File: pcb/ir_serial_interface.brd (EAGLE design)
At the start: 41.6 x 25.4 mm, 27 parts, among them IC1 PIC18F2550_28W, IC2 LP2992, Q2 BC847SMD, T1 SFH303

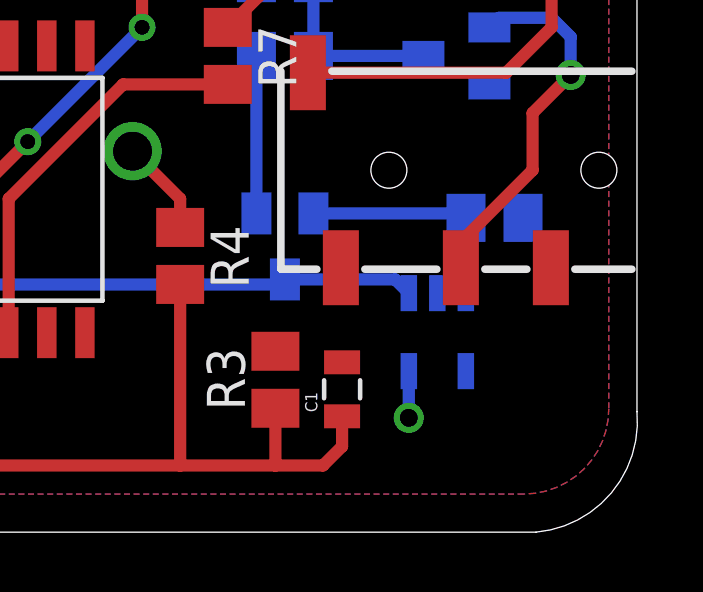
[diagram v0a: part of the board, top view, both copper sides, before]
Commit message: PCB: missing routes
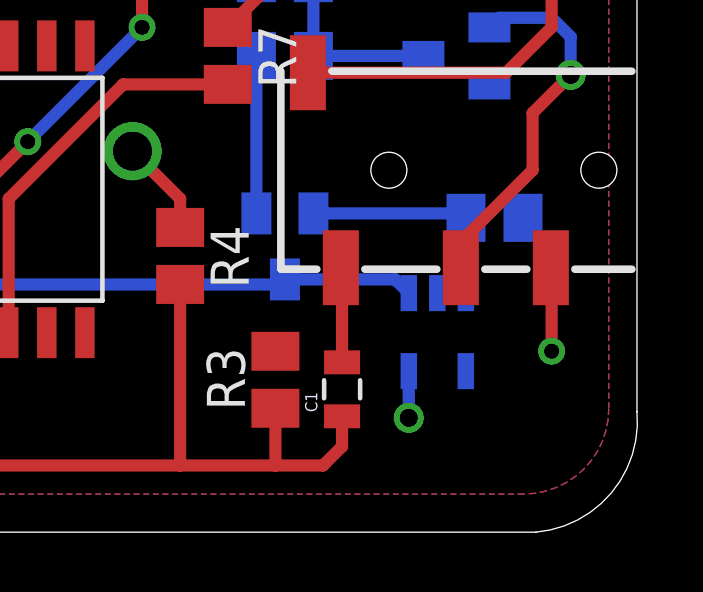
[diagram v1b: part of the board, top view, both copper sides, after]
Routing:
- net N$5: track 0.00 -> 3.19 mm
- net GND: track 23.9 -> 26.7 mm, vias 3 -> 4
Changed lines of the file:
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@@
 <wire x1="46.355" y1="38.1" x2="47.9425" y2="36.5125" width="0.4064" layer="1"/>
 <wire x1="47.9425" y1="36.5125" x2="47.9425" y2="35.5575" width="0.4064" layer="1"/>
-<wire x1="59.37" y1="35.8775" x2="60.3" y2="34.215" width="0" layer="19" extent="1-16"/>
+<wire x1="60.3" y1="34.215" x2="60.325" y2="34.215" width="0.4064" layer="1"/>
+<wire x1="60.325" y1="34.215" x2="60.325" y2="31.4325" width="0.4064" layer="1"/>
+<via x="60.325" y="31.4325" extent="1-16" drill="0.5"/>
 </signal>
 <signal name="N$1">
@@
 <contactref element="U$2" pad="TIP"/>
 <contactref element="C1" pad="2"/>
-<wire x1="53.34" y1="31.0625" x2="53.3" y2="34.215" width="0" layer="19" extent="1-1"/>
+<wire x1="53.3" y1="34.215" x2="53.34" y2="34.215" width="0.4064" layer="1"/>
+<wire x1="53.34" y1="34.215" x2="53.34" y2="31.0625" width="0.4064" layer="1"/>
 </signal>
 <signal name="N$11">

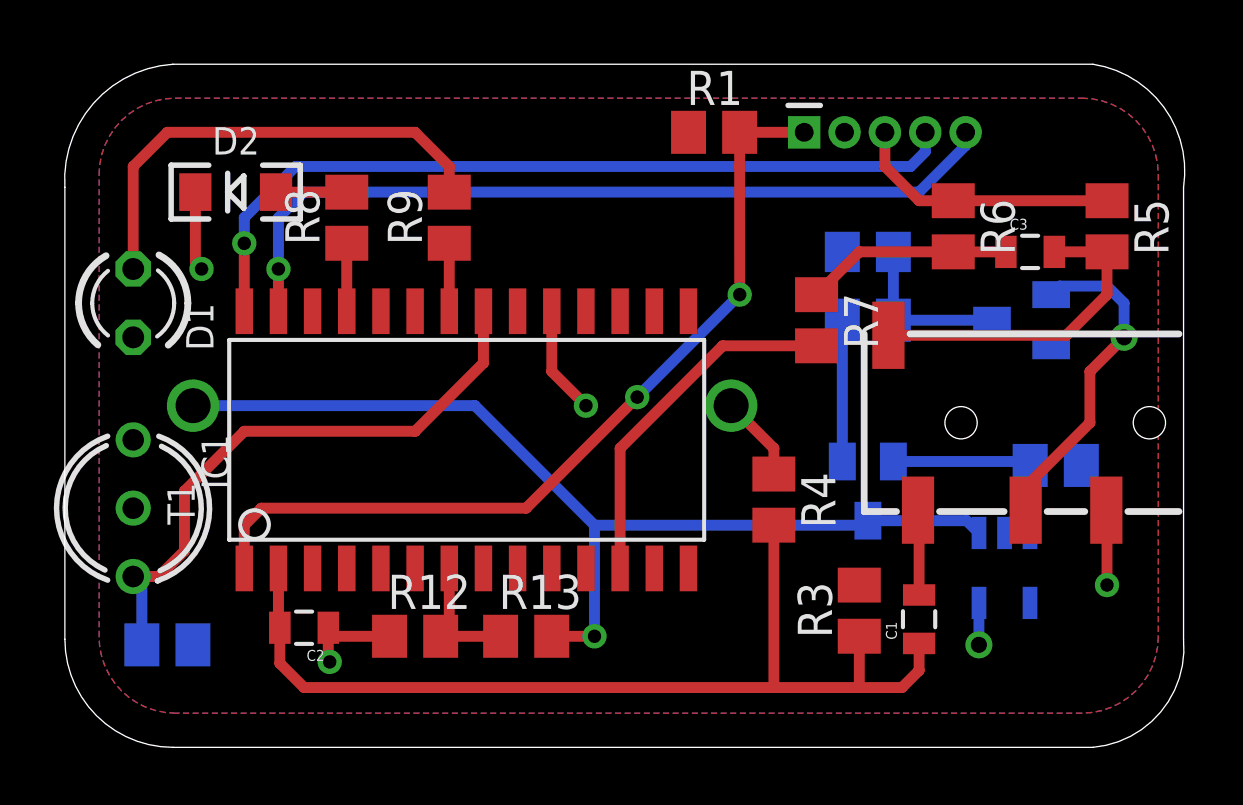
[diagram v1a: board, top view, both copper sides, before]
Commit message: cut round - wider outline path
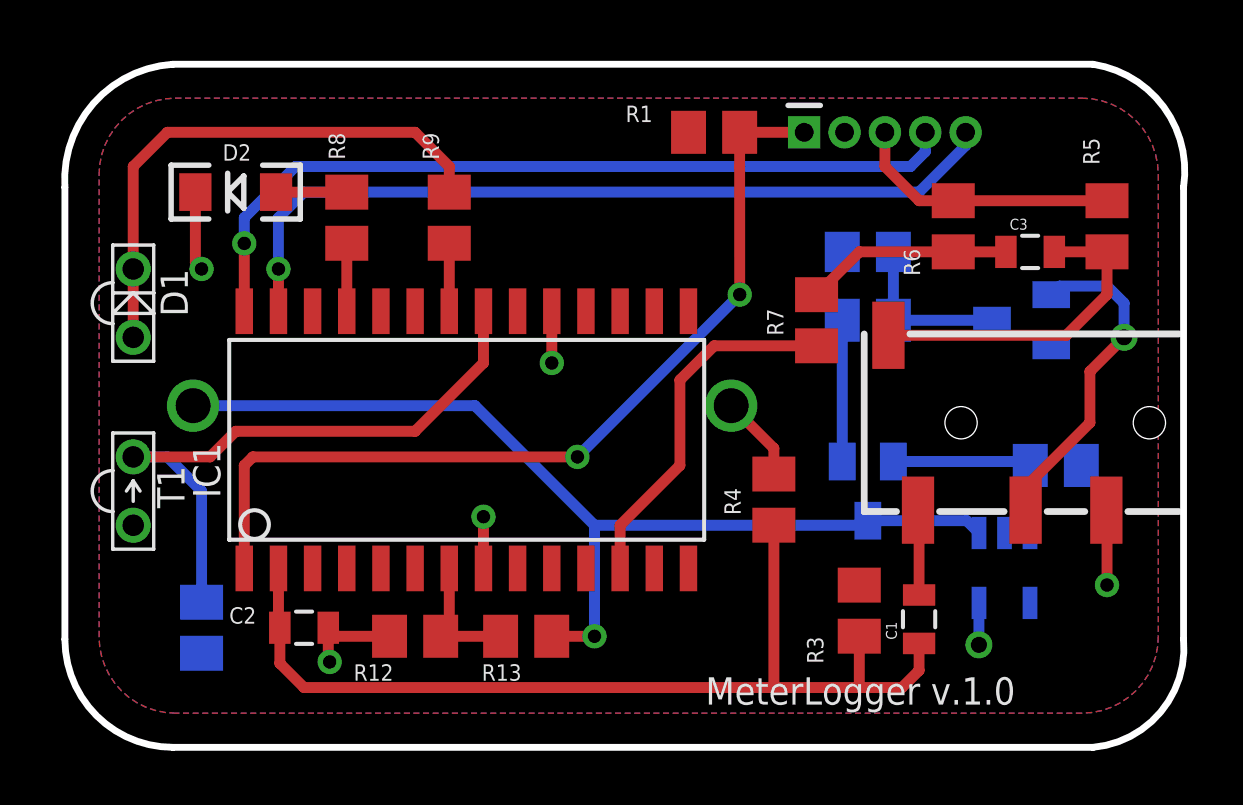
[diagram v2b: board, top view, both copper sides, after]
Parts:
- D1: device led:LED3MM -> SparkFun-LED:LTE-302
- T1: value SFH303 -> PS401; device opto-trans-siemens:SFH303 -> SparkFun-Sensors:LTR-301
- moved R2 1.42 mm to (26.7, 29.8), turned to 90 degrees
- moved T1 0.63 mm to (24.1, 34.9), turned to 270 degrees
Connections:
- removed net VSS: IC1.8
- net +5V: now also T1.C; no longer T1.2
- net GND: now also D1.C, IC1.8; no longer D1.K
- net N$1: now also T1.E; no longer T1.1
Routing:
- net N$14: track 17.6 -> 20.1 mm
- net N$1: track 22.2 -> 23.6 mm
- net N$2: track 32.0 -> 33.3 mm
- net GND: track 26.7 -> 26.6 mm, vias 4 -> 5
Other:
- board text added: "(C) 2014, Kristoffer Ek + Johannes Gaardsted Jørgensen"
- board text added: "2 x CR2032"
- board text added: "MeterLogger v.1.0"

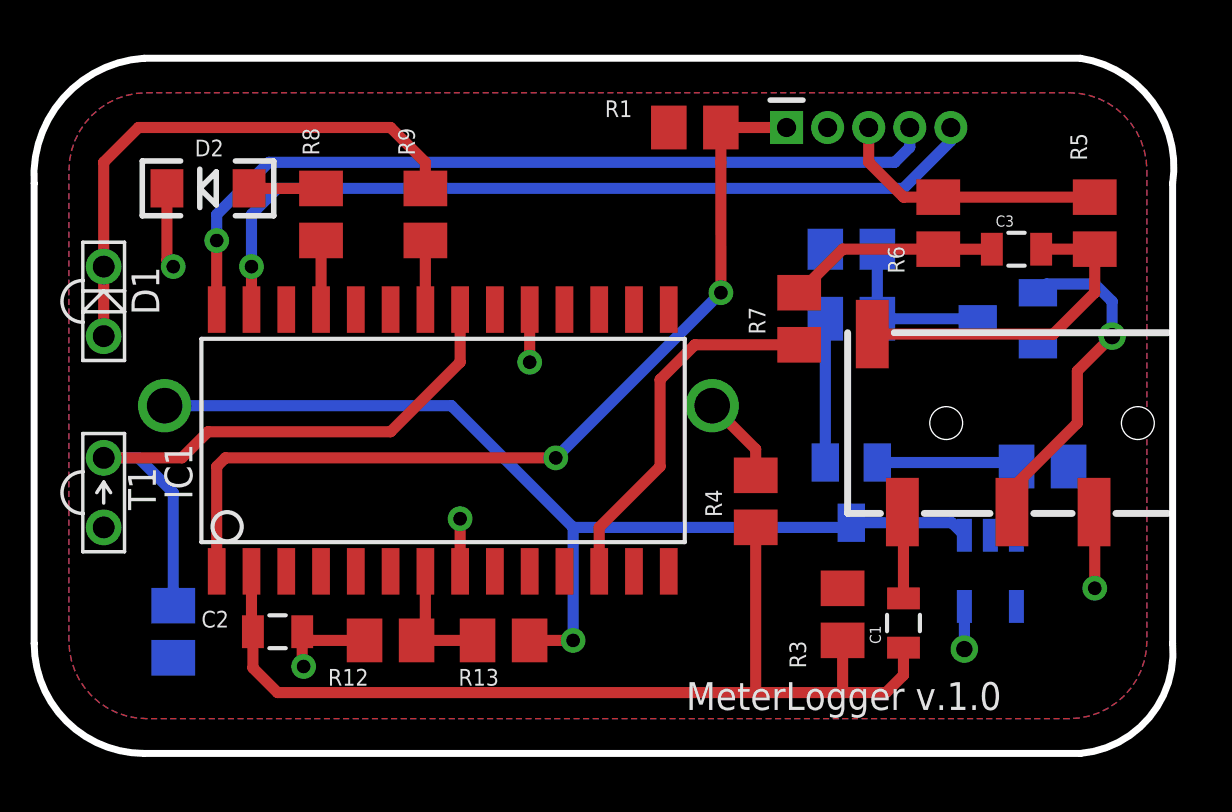
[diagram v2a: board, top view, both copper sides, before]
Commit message: silk screen on name layer not value layer
+ component values
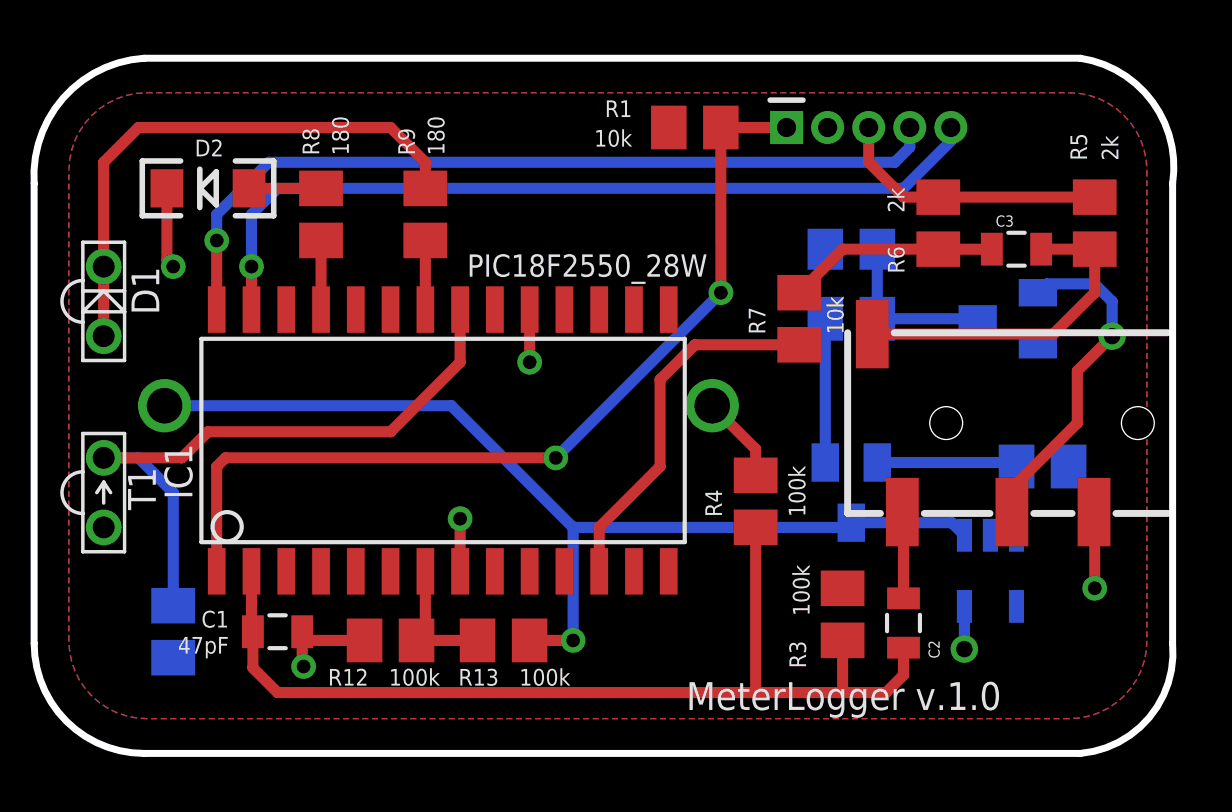
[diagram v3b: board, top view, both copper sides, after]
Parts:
- C1: value 0.2uF -> 47pF
- C2: value 47pF -> 220nF
- C3: value 0.2uF -> 220nF
- C4: value (none) -> 220nF
- D3: value (none) -> BAT65-05; device semicon-smd-ipc:SOT23 -> diode:SOT23
- Q2: value BC847SMD -> MMBT6428LT1G
- R8, R9: value 190 -> 180
- moved C1 22.9 mm to (30.5, 29.8), turned to 180 degrees
- moved C2 22.9 mm to (53.3, 30.2), turned to 90 degrees
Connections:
- net GND: now also C1.1; no longer C2.1
- net N$5: now also C2.2; no longer C1.2
- net N$6: now also C1.2, C2.1; no longer C1.1, C2.2

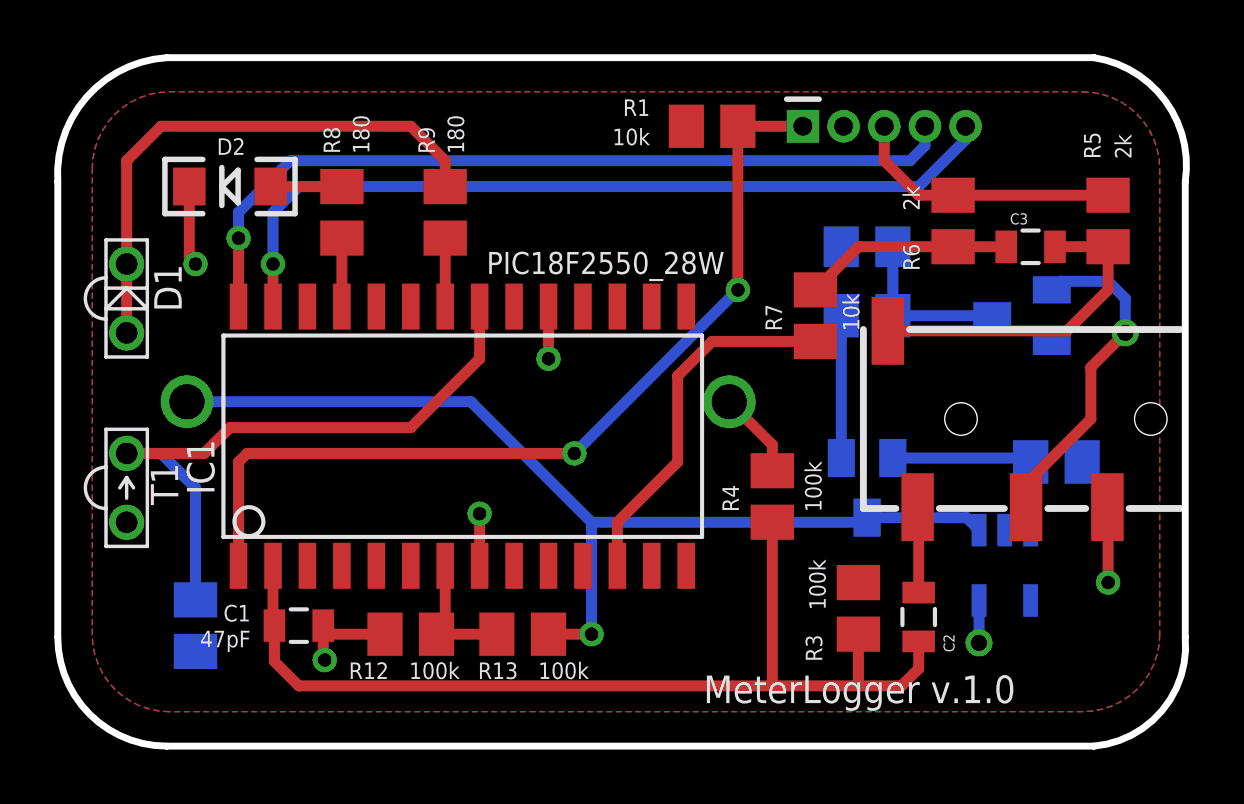
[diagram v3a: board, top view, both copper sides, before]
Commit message: PCB: silk complete
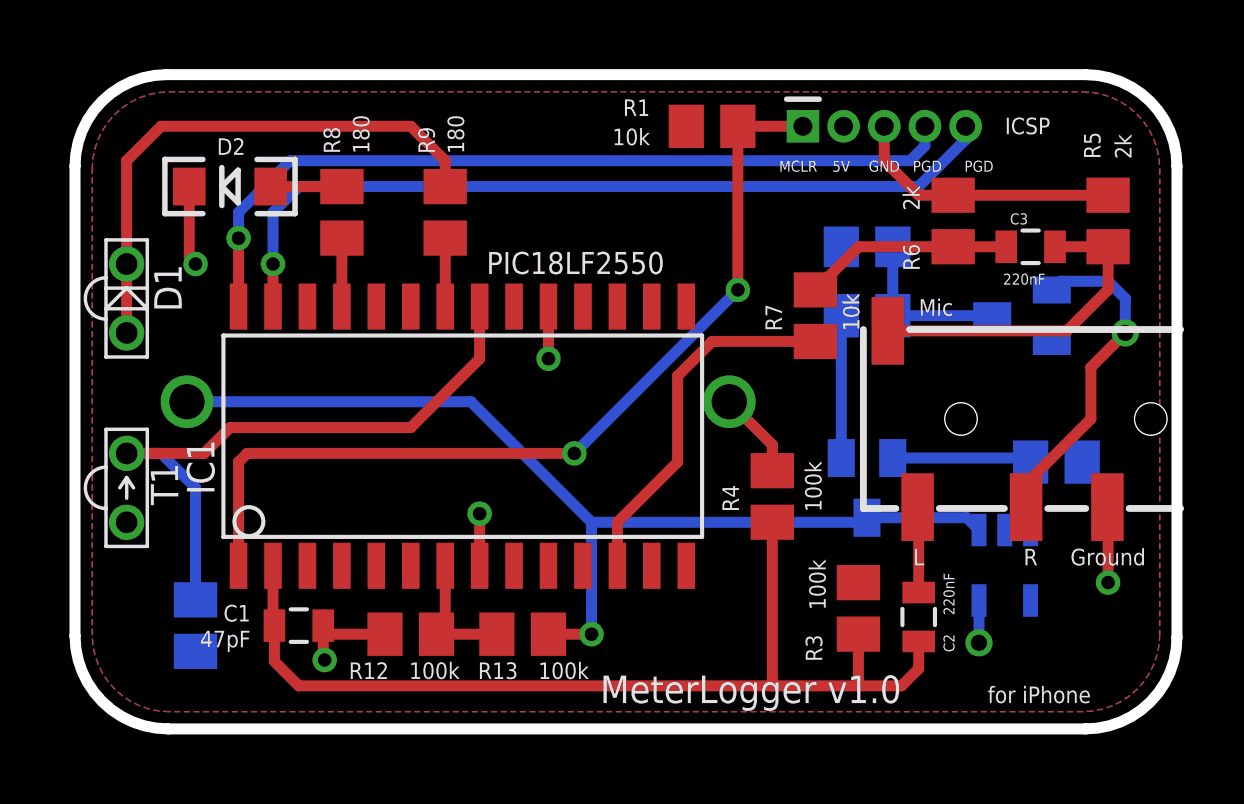
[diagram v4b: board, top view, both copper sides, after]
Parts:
- IC1: value PIC18F2550_28W -> PIC18LF2550
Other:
- board size 41.6 x 25.4 mm -> 40.6 x 24.1 mm
- board text added: "5V"
- board text added: "GND"
- board text added: "Ground"
- board text added: "ICSP"
- board text added: "L"
- board text added: "MCLR"
- board text added: "MeterLogger v1.0"
- board text added: "Mic"
- board text added: "PGD"
- board text added: "R"
- board text added: "for iPhone"
- board text removed: "MeterLogger v.1.0"

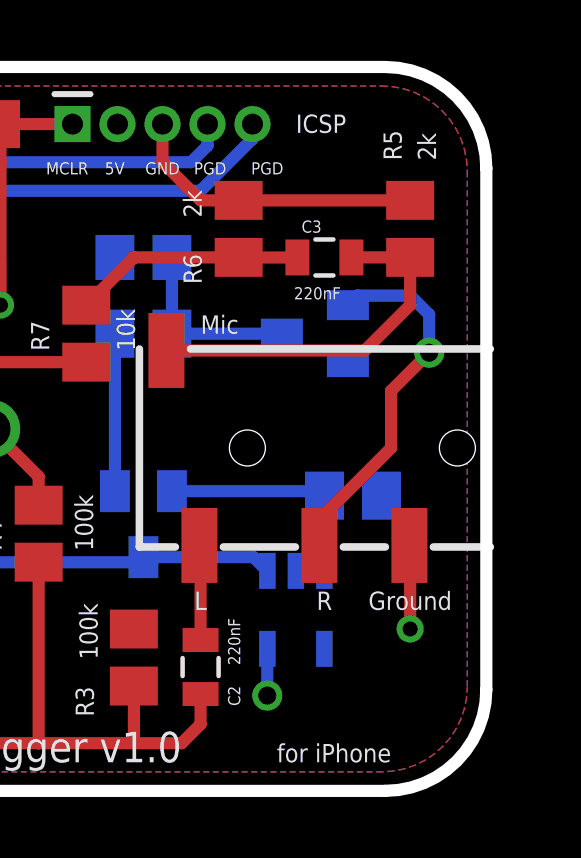
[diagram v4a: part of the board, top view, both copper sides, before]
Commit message: PCB: boad too short
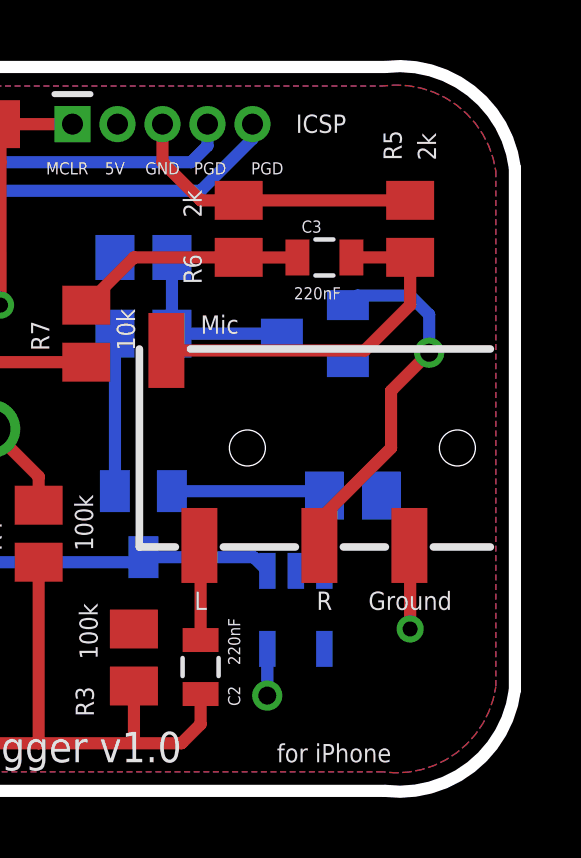
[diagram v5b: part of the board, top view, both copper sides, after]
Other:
- board size 40.6 x 24.1 mm -> 41.6 x 24.2 mm
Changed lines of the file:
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@@
 <layers>
 <layer number="1" name="Top" color="4" fill="1" visible="yes" active="yes"/>
-<layer number="16" name="Bottom" color="1" fill="1" visible="no" active="yes"/>
+<layer number="16" name="Bottom" color="1" fill="1" visible="yes" active="yes"/>
 <layer number="17" name="Pads" color="2" fill="1" visible="yes" active="yes"/>
 <layer number="18" name="Vias" color="2" fill="1" visible="yes" active="yes"/>
@@
 <text x="48.895" y="46.99" size="0.4064" layer="121" ratio="10" rot="R180" align="bottom-center">MCLR</text>
 <wire x1="25.60006875" y1="50.165" x2="59.48993125" y2="50.165" width="0.4064" layer="20"/>
-<wire x1="59.48993125" y1="50.165" x2="62.865" y2="46.78993125" width="0.4064" layer="20" curve="-90"/>
-<wire x1="62.865" y1="46.78993125" x2="62.865" y2="29.41006875" width="0.4064" layer="20"/>
-<wire x1="62.865" y1="29.41006875" x2="59.48993125" y2="26.035" width="0.4064" layer="20" curve="-90"/>
+<wire x1="59.48993125" y1="50.165" x2="63.8175" y2="46.78993125" width="0.4064" layer="20" curve="-90"/>
+<wire x1="63.8175" y1="46.78993125" x2="63.8175" y2="29.41006875" width="0.4064" layer="20"/>
+<wire x1="63.8175" y1="29.41006875" x2="59.48993125" y2="26.035" width="0.4064" layer="20" curve="-90"/>
 <wire x1="59.48993125" y1="26.035" x2="25.6592875" y2="26.035" width="0.4064" layer="20"/>
 <wire x1="25.6592875" y1="26.035" x2="22.225" y2="29.4692875" width="0.4064" layer="20" curve="-90"/>
@@
 <vertex x="25.69980625" y="49.53"/>
 <vertex x="59.39019375" y="49.53" curve="-90"/>
-<vertex x="62.23" y="46.69019375"/>
-<vertex x="62.23" y="29.50980625" curve="-90"/>
+<vertex x="63.1825" y="46.69019375"/>
+<vertex x="63.1825" y="29.50980625" curve="-90"/>
 <vertex x="59.39019375" y="26.67"/>
 <vertex x="25.69980625" y="26.67" curve="-90"/>
@@
 <vertex x="25.69980625" y="49.53"/>
 <vertex x="59.39019375" y="49.53" curve="-90"/>
-<vertex x="62.23" y="46.69019375"/>
-<vertex x="62.23" y="29.50980625" curve="-90"/>
+<vertex x="63.1825" y="46.69019375"/>
+<vertex x="63.1825" y="29.50980625" curve="-90"/>
 <vertex x="59.39019375" y="26.67"/>
 <vertex x="25.69980625" y="26.67" curve="-90"/>
